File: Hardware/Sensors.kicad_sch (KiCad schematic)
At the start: 56 parts, among them J10 VL530X Connector, J11 VL530X Connector, J12 VL530X Connector, J13 VL530X Connector, J14 BNO085 Breakout, J5 Conn_01x08_Pin, J8 VL530X Connector, J9 VL530X Connector, Q10 Q_NMOS_GSD, Q11 Q_NMOS_GSD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

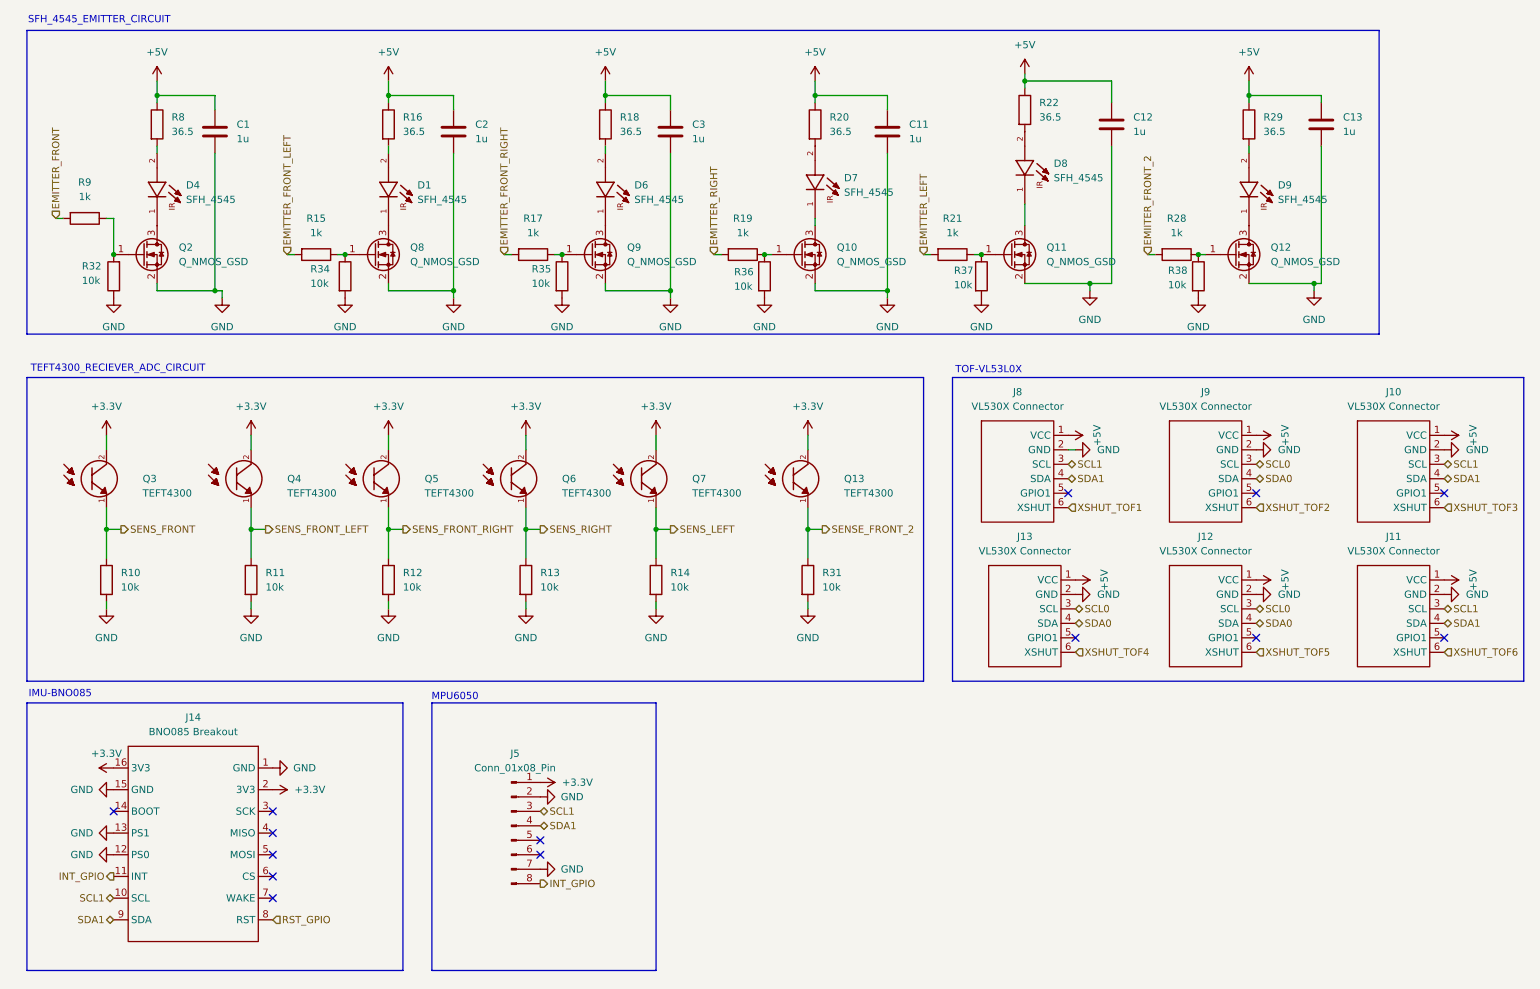
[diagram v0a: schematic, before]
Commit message: Updated PCB files after dfm check
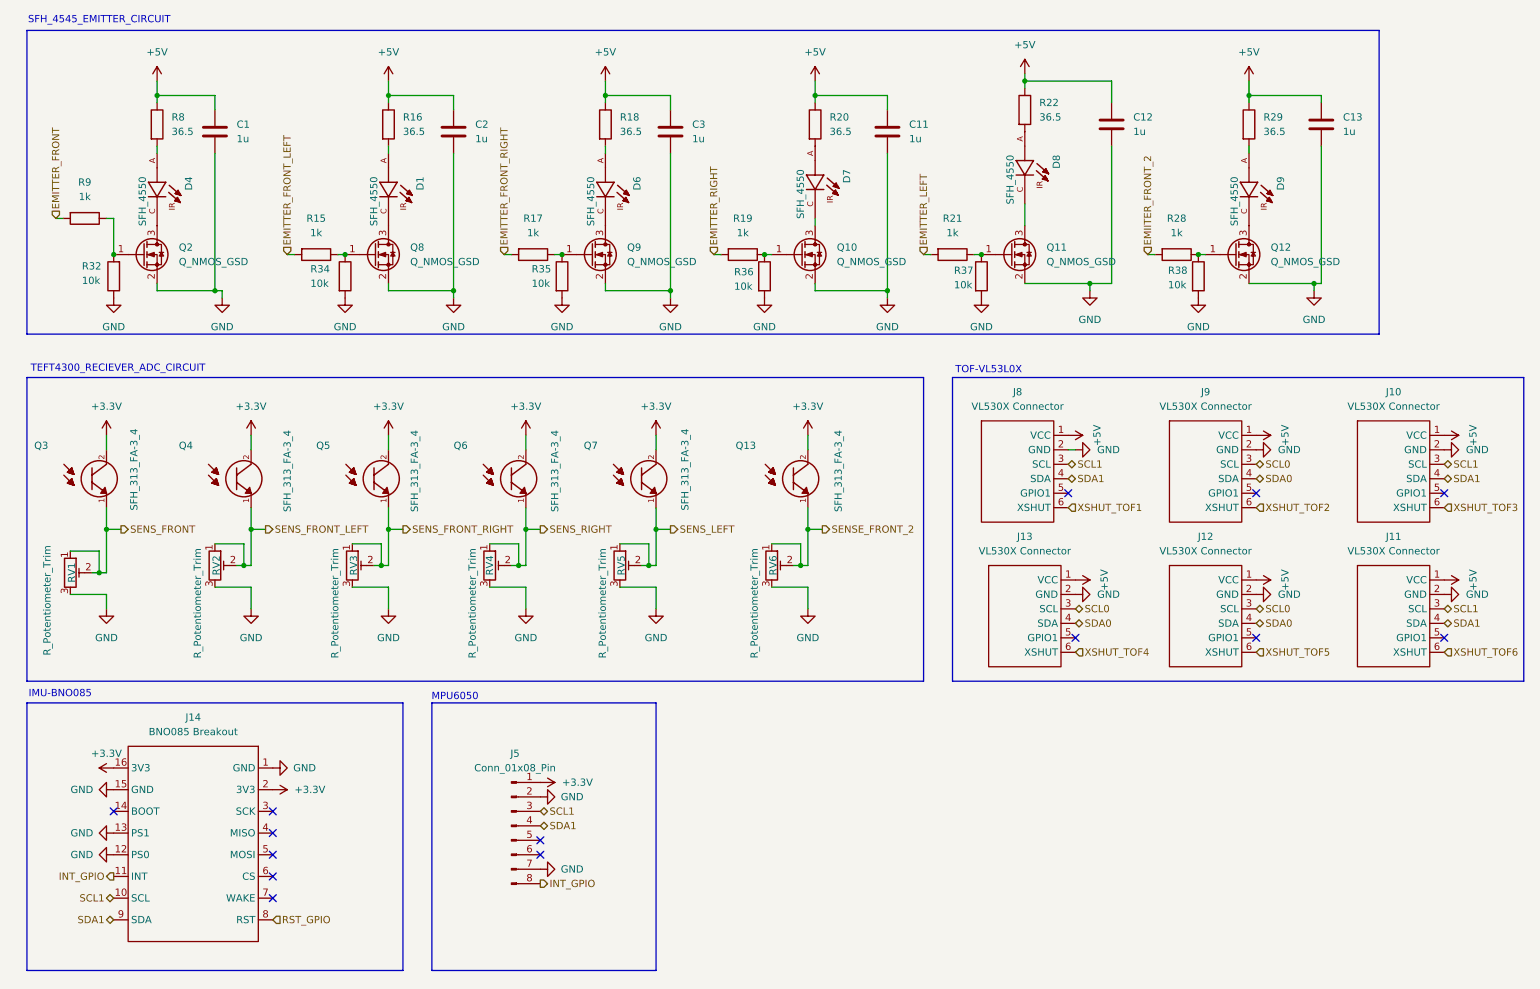
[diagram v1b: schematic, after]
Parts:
- removed R10, R11, R12, R13, R14, R31: 10k, Resistor_SMD:R_0603_1608Metric_Pad0.98x0.95mm_HandSolder, symbol Device:R
- added RV1, RV2, RV3, RV4, RV5, RV6: R_Potentiometer_Trim, Potentiometer_THT:Potentiometer_Bourns_3296W_Vertical, symbol Device:R_Potentiometer_Trim
- D1, D4, D6, D7, D8, D9: value SFH_4545 -> SFH_4550; footprint SFH_4545:DIO_SFH_4545 -> SFH_4550:DIO_SFH_4550; symbol SFH_4545:SFH_4545 -> SFH_4550:SFH_4550; Check_prices https://www.snapeda.com/parts/SFH%204545/Osram/view-part/?r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 -> https://www.snapeda.com/parts/SFH%204550/Osram/view-part/?r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; MP SFH 4545 -> SFH 4550; PARTREV 1.5 -> 1.6; Package None -> Radial Osram Opto; SnapEDA_Link https://www.snapeda.com/parts/SFH%204545/Osram/view-part/?r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 -> https://www.snapeda.com/parts/SFH%204550/Osram/view-part/?r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
- Q13, Q3, Q4, Q5, Q6, Q7: value TEFT4300 -> SFH_313_FA-3_4; footprint TEFT4300 (2):XDCR_TEFT4300 -> SFH_313_FA-3_4:XDCR_SFH_313_FA-3_4; symbol TEFT4300:TEFT4300 -> SFH_313_FA-3_4:SFH_313_FA-3_4; Check_prices https://www.snapeda.com/parts/TEFT4300/Vishay/view-part/?re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 -> https://www.snapeda.com/parts/SFH%20313%20FA-3/4/Osram/view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; MANUFACTURER (none) -> OSRAM; MF Vishay Semiconductor -> OSRAM Opto; MP TEFT4300 -> SFH 313 FA-3/4; PARTREV (none) -> 1.3; Package None -> Radial-2 OSRAM Opto; STANDARD (none) -> Manufacturer Recommendations; SnapEDA_Link https://www.snapeda.com/parts/TEFT4300/Vishay/view-part/?re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 -> https://www.snapeda.com/parts/SFH%20313%20FA-3/4/Osram/view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
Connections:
- net GND: now also RV1.3, RV2.3, RV3.3, RV4.3, RV5.3, RV6.3
- net SENSE_FRONT_2: now also RV6.1, RV6.2
- net SENS_FRONT: now also RV1.1, RV1.2
- net SENS_FRONT_LEFT: now also RV2.1, RV2.2
- net SENS_FRONT_RIGHT: now also RV3.1, RV3.2
- net SENS_LEFT: now also RV5.1, RV5.2
- net SENS_RIGHT: now also RV4.1, RV4.2
- net at R8.2: now also D4.A; no longer D4.2
- net at Q9.3 (D): now also D6.C; no longer D6.1
- net at Q8.3 (D): now also D1.C; no longer D1.1
- net at R16.2: now also D1.A; no longer D1.2
- net at Q10.3 (D): now also D7.C; no longer D7.1
- net at Q2.3 (D): now also D4.C; no longer D4.1
- net at R29.2: now also D9.A; no longer D9.2
- net at R20.2: now also D7.A; no longer D7.2
- net at Q12.3 (D): now also D9.C; no longer D9.1
- net at Q11.3 (D): now also D8.C; no longer D8.1
- net at R22.2: now also D8.A; no longer D8.2
- net at R18.2: now also D6.A; no longer D6.2

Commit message: Made changes with i2c bus, added state connection and removed en of hc05, added bno085 fuse,bno085 2nd 3v3 unconnected flag has been put, reversed the connection for battery connector based on the xt30 signs,removed all daisy chained power traces and made it into start topology, fiexd drc erros,dfm check erros
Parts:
- added F1: Polyfuse, Fuse:Fuse_0805_2012Metric_Pad1.15x1.40mm_HandSolder, symbol Device:Polyfuse
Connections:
- net +3.3V: now also F1.2; no longer J14.16 (3V3), J14.2 (3V3)
- new net: F1.1, J14.16 (3V3)
- no-connect marks 14 -> 15
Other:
- note added: "EMITTER_CIRCUIT"
- note added: "RECIEVER_ADC_CIRCUIT"
- note removed: "SFH_4545_EMITTER_CIRCUIT"
- note removed: "TEFT4300_RECIEVER_ADC_CIRCUIT"
- moved on the sheet: J14
